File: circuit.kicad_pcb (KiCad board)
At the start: 2 copper layers, 70.7 x 56.6 mm, 9 parts

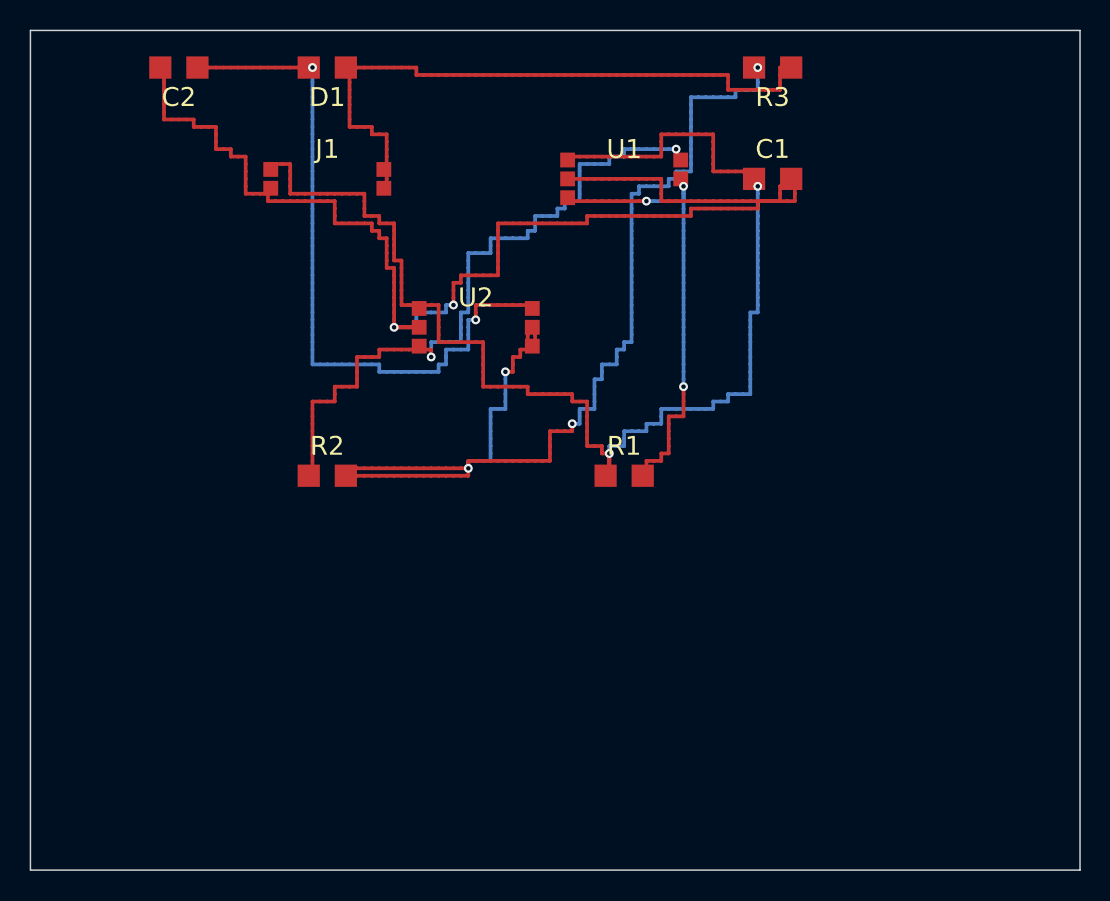
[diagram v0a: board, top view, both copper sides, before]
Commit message: fix: v0.5.2 — KiCad pin-transform authority + net-derivation fidelity + schematic best-practice checks
Validation round: live-probed KiCad 10.0.6 itself with a 4-pin symbol
at instance rot 0 and rot 90, all four pin directions. AUTHORITATIVE
transform: a lib pin (px,py) renders at origin + R(-rot)·(px,-py) —
mirror the lib Y, then rotate by MINUS the instance rotation. The
v0.4.2 'mirror-only' inference was rot-0-only evidence; the earlier
mirror-then-rotate-by-+rot double-flipped rot-180 pins onto their
neighbors (found by the decoupling test).

NET DERIVATION FIDELITY (live-verified against kicad-cli's own netlist):
- point-on-segment connection added so labels attach anywhere along a
  wire (midpoint labels previously produced unnamed nets)
- scoped to labels/no-connects only: KiCad connects PINS to wires only
  at wire ENDPOINTS — a wire passing through a pin position is NOT a
  connection (the generated 555's long vertical drops pass near other
  pins; the unscoped test merged every net into one)
- HashMap key type bug in the decoupling check fixed (a &String key vs
  &str lookup silently returned 0 and disabled the check)

SCHEMATIC BEST PRACTICE (per the harness directive):
- missing-decoupling ERC check: an IC power net without a capacitor
  flags with the skill-102 guidance (100nF within 2mm) — the cap
  heuristic now matches the lib type suffix ('Device:C' yes, 'Device:R'
  no — the word 'Device' itself contains a 'C' and false-positived)
- physics-driven placement intent: components ≥0.5W get apart ≥15mm
  separation via the placer's constraint solver

E2E verified on all three fixtures: nets derived correctly (555: VCC/
GND/OUT separate), decoupling fires where caps are absent (555, RF)
and stays silent where present (stress), kicad-cli DRC 0 unconnected +
0 electrical on all three, KiCad reads 7 correct nets from the stress
schematic's exported netlist.

151/151 tests.
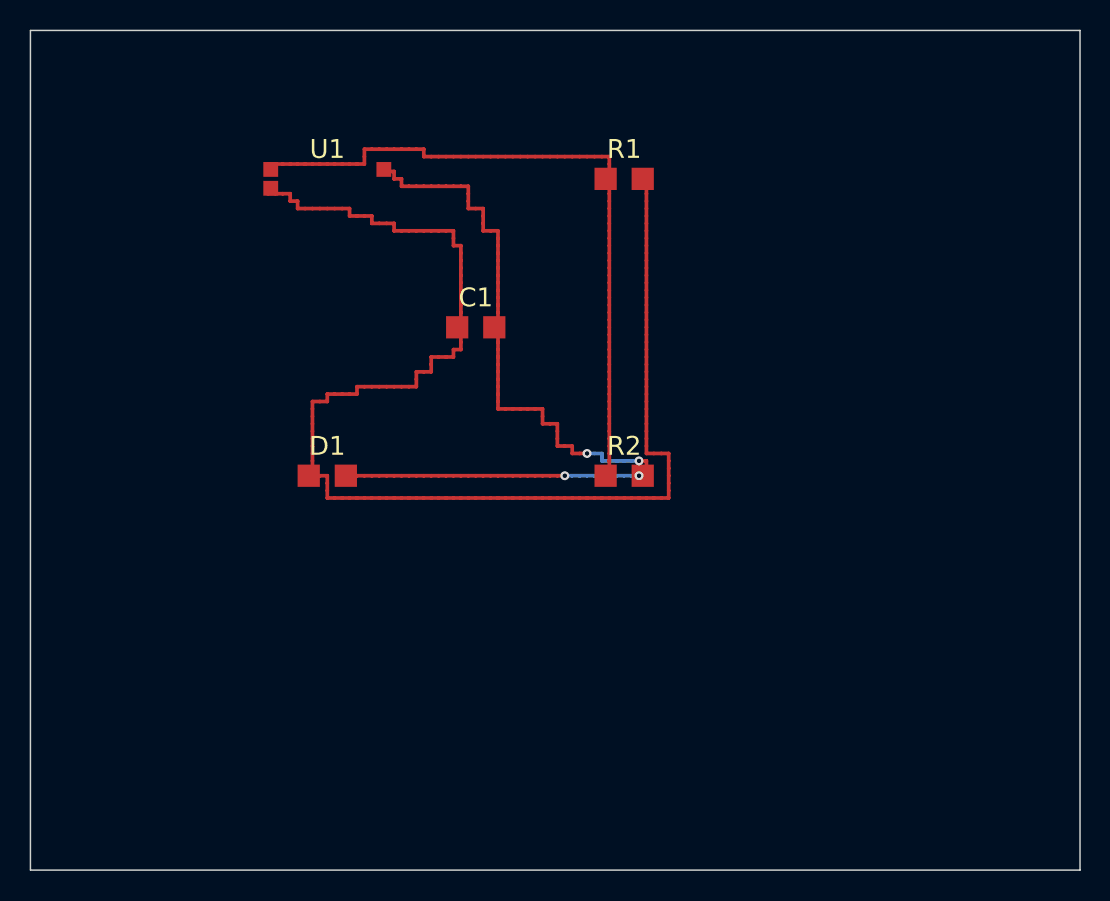
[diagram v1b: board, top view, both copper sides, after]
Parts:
- removed C2: , Capacitor_SMD:C_0805
- removed J1: , Connector:PinHeader_1x04
- removed R3: , Resistor_SMD:R_0603
- removed U2: , Package_SO:SOIC-14
- C1: footprint Capacitor_SMD:C_0603 -> Capacitor_SMD:C_0805_2012Metric
- D1: footprint Diode_SMD:D_SOD-123 -> LED_SMD:LED_0805_2012Metric
- R1: footprint Resistor_SMD:R_0603 -> Resistor_SMD:R_0603_1608Metric
- R2: footprint Resistor_SMD:R_0603 -> Resistor_SMD:R_0805_2012Metric
- U1: footprint Package_SO:SOIC-8 -> Package_DIP:DIP-8_W7.62mm
- moved D1 27.5 mm to (20.0, 30.0)
- moved C1 22.4 mm to (30.0, 20.0)
- moved R1 20.0 mm to (40.0, 10.0)
- moved R2 20.0 mm to (40.0, 30.0)
- moved U1 20.0 mm to (20.0, 10.0)
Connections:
- C1 pad 1: VCC -> OUT
- D1 pad 1: N4 -> OUT
- D1 pad 2: N5 -> GND
- R1 pad 2: N1 -> GND
- R2 pad 1: N2 -> VCC
- R2 pad 2: N3 -> OUT
- U1 pad 1: N1 -> VCC
- U1 pad 3: N2 -> OUT
- U1 pad 8: VCC -> GND
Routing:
- net N3: track 79.0 -> 0.00 mm, vias 4 -> 0
- net OUT: track 0.00 -> 58.0 mm, vias 0 -> 4
- net N2: track 48.5 -> 0.00 mm, vias 2 -> 0
- net N4: track 47.5 -> 0.00 mm, vias 2 -> 0
- net VCC: track 92.0 -> 46.5 mm, vias 2 -> 0
- net N5: track 43.5 -> 0.00 mm
- net N1: track 32.0 -> 0.00 mm, vias 3 -> 0
- net GND: track 92.5 -> 91.0 mm, vias 2 -> 0
